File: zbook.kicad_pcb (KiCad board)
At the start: 4 copper layers, 77 x 89 mm, 170 parts, among them J1 USB_C_Receptacle_USB2.0_16P, J2 USB_C_Receptacle_USB2.0_16P, J3 Conn_01x05_Pin, J4 Conn_01x05_Pin, J5 Conn_02x04_Odd_Even, J6 Conn_02x15_Counter_Clockwise, J7 MSD-4-A, J8 DISPLAY CONN, Q1 T2N7002AK,LM, Q2 FDN327N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

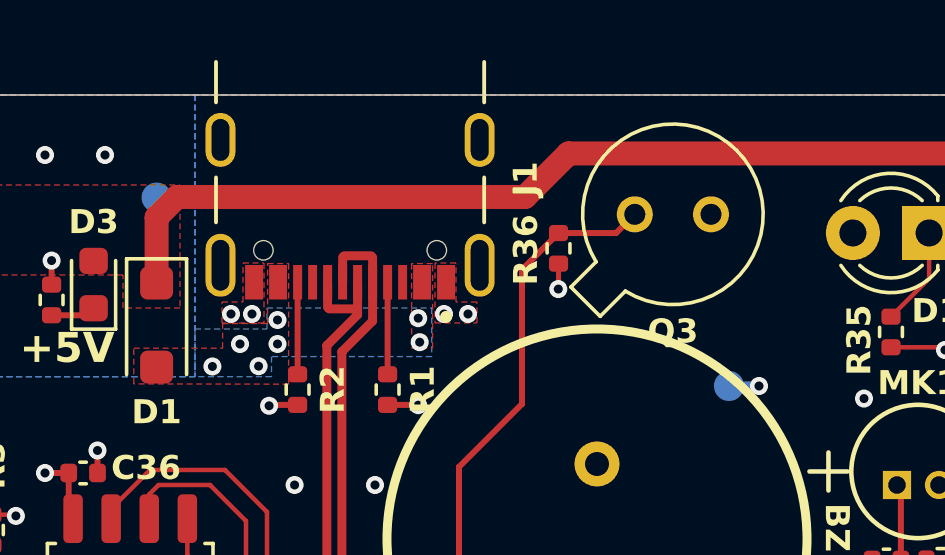
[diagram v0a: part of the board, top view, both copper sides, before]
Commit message: fix: changes phototransistor footprint
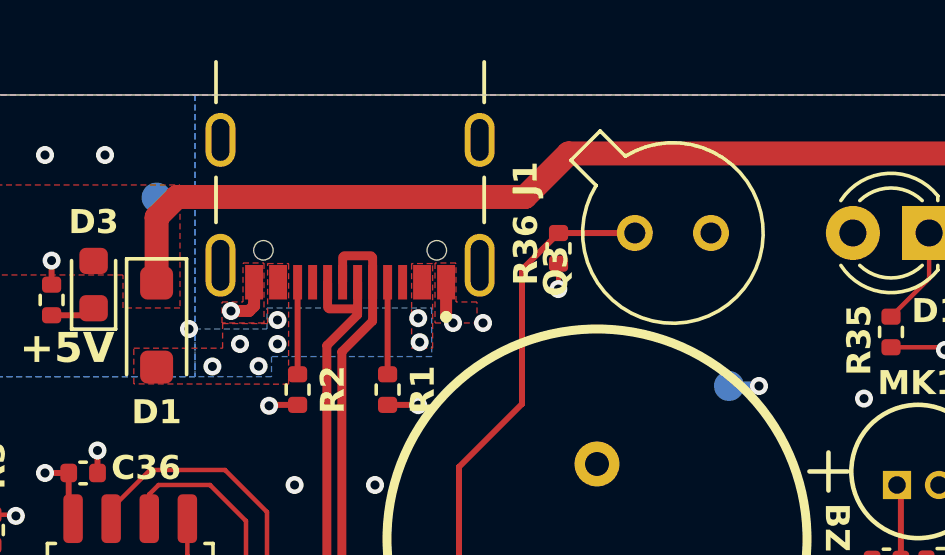
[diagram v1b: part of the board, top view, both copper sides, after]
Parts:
- moved Q3 1.41 mm to (155.9, 68.6), turned to -90 degrees
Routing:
- net GND: track 109.5 -> 112.6 mm
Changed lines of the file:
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@@
 	(footprint "peripherals1:TO-18-2"
 		(layer "F.Cu")
-		(at 154.66 67.978039)
+		(at 155.93 68.6 -90)
 		(descr "TO-18-2, generated with kicad-footprint-generator TO_SOT_THT_generate.py")
 		(tags "TO-18-2")
 		(property "Reference" "Q3"
-			(at 1.27 3.9 0)
+			(at 1.27 3.9 90)
 			(layer "F.SilkS")
 			(effects
@@
 		)
 		(property "Value" "Q_Photo_NPN"
-			(at 1.27 4.01 0)
+			(at 1.27 4.01 90)
 			(layer "F.Fab")
 			(effects
@@
 			)
 		)
-		(property "Datasheet" "https://www.digikey.com.br/pt/products/detail/tt-electronics-optek-technology/OP598A/498701?s=N4IgTCBcDaIPIAUCsBOAHAQRAXQL5A"
-			(at 0 0 0)
+		(property "Datasheet" "https://www.digikey.com.br/en/products/detail/tt-electronics-optek-technology/OP598A/498701?s=N4IgTCBcDaIPIAUCsBOAHAQRAXQL5A"
+			(at 0 0 90)
 			(layer "F.Fab")
 			(hide yes)
@@
 			)
 		)
-		(property "Description" "Phototransistor"
-			(at 0 0 0)
+		(property "Description" "NPN phototransistor, collector/emitter"
+			(at 0 0 90)
 			(layer "F.Fab")
 			(hide yes)
@@
 		)
 		(property "MPN" "OP598A"
-			(at 0 0 0)
+			(at 0 0 270)
 			(unlocked yes)
 			(layer "F.Fab")
@@
 		)
 		(property "Availability" ""
-			(at 0 0 0)
+			(at 0 0 270)
 			(unlocked yes)
 			(layer "F.Fab")
@@
 		)
 		(property "Check_prices" ""
-			(at 0 0 0)
+			(at 0 0 270)
 			(unlocked yes)
 			(layer "F.Fab")
@@
 		)
 		(property "Description_1" ""
-			(at 0 0 0)
+			(at 0 0 270)
 			(unlocked yes)
 			(layer "F.Fab")
@@
 		)
 		(property "MF" ""
-			(at 0 0 0)
+			(at 0 0 270)
 			(unlocked yes)
 			(layer "F.Fab")
@@
 		)
 		(property "Package" ""
-			(at 0 0 0)
+			(at 0 0 270)
 			(unlocked yes)
 			(layer "F.Fab")
@@
 		)
 		(property "Price" ""
-			(at 0 0 0)
+			(at 0 0 270)
 			(unlocked yes)
 			(layer "F.Fab")
@@
 		)
 		(property "SnapEDA_Link" ""
-			(at 0 0 0)
+			(at 0 0 270)
 			(unlocked yes)
 			(layer "F.Fab")
@@
 		(attr through_hole)
 		(fp_line
-			(start -2.130108 2.424301)
-			(end -1.154301 3.400108)
+			(start -2.424301 3.400108)
+			(end -1.583811 2.559618)
 			(stroke
 				(width 0.12)
@@
 		)
 		(fp_line
-			(start -1.289618 1.583811)
-			(end -2.130108 2.424301)
+			(start -3.400108 2.424301)
+			(end -2.424301 3.400108)
 			(stroke
 				(width 0.12)
@@
 		)
 		(fp_line
-			(start -1.154301 3.400108)
-			(end -0.313811 2.559618)
+			(start -2.559618 1.583811)
+			(end -3.400108 2.424301)
 			(stroke
 				(width 0.12)
@@
 		)
 		(fp_arc
-			(start -1.289618 1.583811)
-			(mid 3.398392 -2.128392)
-			(end -0.313811 2.559618)
+			(start -2.559618 1.583811)
+			(mid 2.128392 -2.128392)
+			(end -1.583811 2.559618)
 			(stroke
 				(width 0.12)
@@
 		)
 		(fp_line
-			(start -2.323922 2.420125)
-			(end -1.150125 3.593922)
+			(start -2.420125 3.593922)
+			(end -1.561775 2.735573)
 			(stroke
 				(width 0.05)
@@
 		)
 		(fp_line
-			(start -1.465573 1.561775)
-			(end -2.323922 2.420125)
+			(start -3.593922 2.420125)
+			(end -2.420125 3.593922)
 			(stroke
 				(width 0.05)
@@
 		)
 		(fp_line
-			(start -1.150125 3.593922)
-			(end -0.291775 2.735573)
+			(start -2.735573 1.561775)
+			(end -3.593922 2.420125)
 			(stroke
 				(width 0.05)
@@
 		)
 		(fp_arc
-			(start -1.465573 1.561775)
-			(mid 3.497386 -2.227386)
-			(end -0.291775 2.735573)
+			(start -2.735573 1.561775)
+			(mid 2.227386 -2.227386)
+			(end -1.561775 2.735573)
 			(stroke
 				(width 0.05)
@@
 		)
 		(fp_line
-			(start -1.976616 2.426372)
-			(end -1.156372 3.246616)
+			(start -2.426372 3.246616)
+			(end -1.599057 2.419301)
 			(stroke
 				(width 0.1)
@@
 		)
 		(fp_line
-			(start -1.156372 3.246616)
-			(end -0.329057 2.419301)
+			(start -3.246616 2.426372)
+			(end -2.426372 3.246616)
 			(stroke
 				(width 0.1)
@@
 		)
 		(fp_line
-			(start -1.149301 1.599057)
-			(end -1.976616 2.426372)
+			(start -2.419301 1.599057)
+			(end -3.246616 2.426372)
 			(stroke
 				(width 0.1)
@@
 		)
 		(fp_arc
-			(start -1.149301 1.599057)
-			(mid 3.32061 -2.05061)
-			(end -0.329057 2.419301)
+			(start -2.419301 1.599057)
+			(mid 2.05061 -2.05061)
+			(end -1.599057 2.419301)
 			(stroke
 				(width 0.1)
@@
 		)
 		(fp_circle
-			(center 1.27 0)
-			(end 3.67 0)
+			(center 0 0)
+			(end 2.4 0)
 			(stroke
 				(width 0.1)
@@
 		)
 		(fp_text user "${REFERENCE}"
-			(at 1.27 -4.01 0)
+			(at 1.27 -4.01 90)
 			(layer "F.Fab")
 			(effects
@@
 		)
 		(pad "1" thru_hole circle
-			(at 2.54 0)
+			(at 0 -1.27 270)
 			(size 1.2 1.2)
 			(drill 0.7)
@@
 			(pinfunction "C")
 			(pintype "passive")
-			(zone_connect 1)
 		)
 		(pad "2" thru_hole circle
-			(at 0 0)
+			(at 0 1.27 270)
 			(size 1.2 1.2)
 			(drill 0.7)
@@
 		)
 		(embedded_fonts no)
-		(model "${KICAD9_3DMODEL_DIR}/Package_TO_SOT_THT.3dshapes/TO-18-2.step"
+		(model "${KIPRJMOD}/Libraries/Peripherals1/OP598A.STEP"
 			(offset
-				(xyz 0 0 0)
+				(xyz 0 0 2)
 			)
 			(scale
@@
 			)
 			(rotate
-				(xyz 0 0 0)
+				(xyz -90 -0 -0)
 			)
 		)
@@
 	)
 	(segment
+		(start 148.37 71.37)
+		(end 148.6 71.6)
+		(width 0.4)
+		(layer "F.Cu")
+		(net 1)
+	)
+	(segment
+		(start 141.8 71.2)
+		(end 141.2 71.2)
+		(width 0.4)
+		(layer "F.Cu")
+		(net 1)
+	)
+	(segment
 		(start 144.785 106.055)
 		(end 144.74 106.01)
@@
 	)
 	(segment
+		(start 148.37 70.2425)
+		(end 148.37 71.37)
+		(width 0.4)
+		(layer "F.Cu")
+		(net 1)
+	)
+	(segment
 		(start 146.87 142.39)
 		(end 146.88 142.38)
@@
 	)
 	(segment
+		(start 141.97 70.2425)
+		(end 141.97 71.03)
+		(width 0.4)
+		(layer "F.Cu")
+		(net 1)
+	)
+	(segment
 		(start 137.28 101.05)
 		(end 136.55 101.05)
@@
 	)
 	(segment
+		(start 141.97 71.03)
+		(end 141.8 71.2)
+		(width 0.4)
+		(layer "F.Cu")
+		(net 1)
+	)
+	(segment
 		(start 128.950001 73.1)
 		(end 128.950001 74.430966)
@@
 	)
 	(via
-		(at 141.2 71.3)
+		(at 139.8 71.8)
 		(size 0.6)
 		(drill 0.3)
@@
 	)
 	(via
-		(at 141.9 71.3)
+		(at 141.2 71.2)
 		(size 0.6)
 		(drill 0.3)
@@
 	)
 	(via
-		(at 149.1 71.3)
+		(at 149.6 71.6)
 		(size 0.6)
 		(drill 0.3)
@@
 	)
 	(via
-		(at 148.3 71.3)
+		(at 148.6 71.6)
 		(size 0.6)
 		(drill 0.3)
@@
 	)
 	(segment
-		(start 152.118039 68.601961)
-		(end 154.036078 68.601961)
-		(width 0.2)
-		(layer "F.Cu")
-		(net 109)
-	)
-	(segment
 		(start 151.6 88.3)
 		(end 151.6 86.75)
@@
 	)
 	(segment
-		(start 154.036078 68.601961)
-		(end 154.66 67.978039)
+		(start 154.658039 68.601961)
+		(end 154.66 68.6)
+		(width 0.2)
+		(layer "F.Cu")
+		(net 109)
+	)
+	(segment
+		(start 152.118039 68.601961)
+		(end 154.658039 68.601961)
 		(width 0.2)
 		(layer "F.Cu")

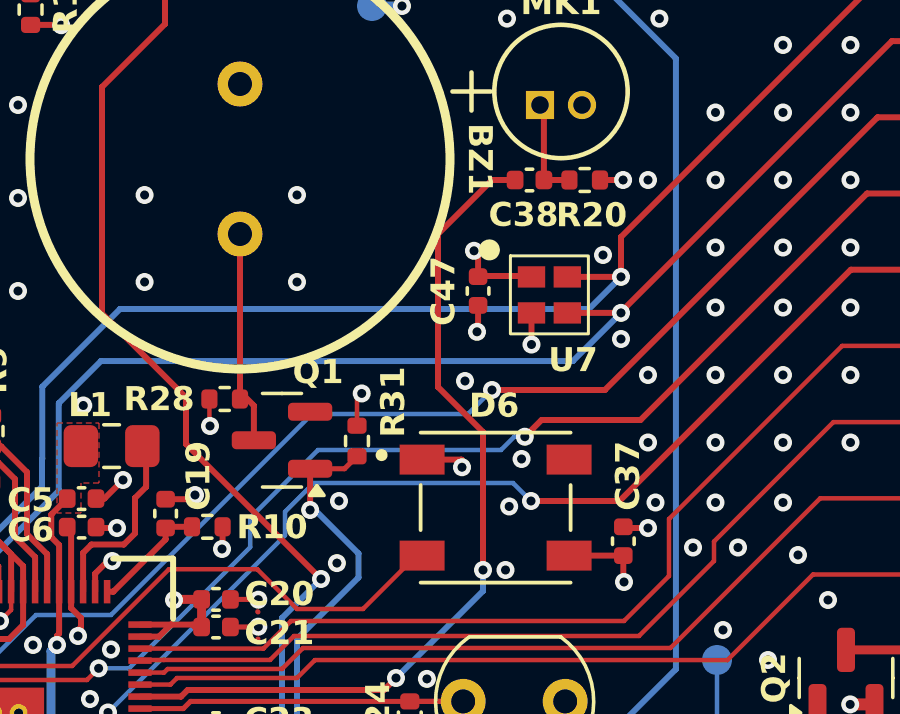
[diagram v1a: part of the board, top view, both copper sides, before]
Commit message: fix: fixes header table behind pcb
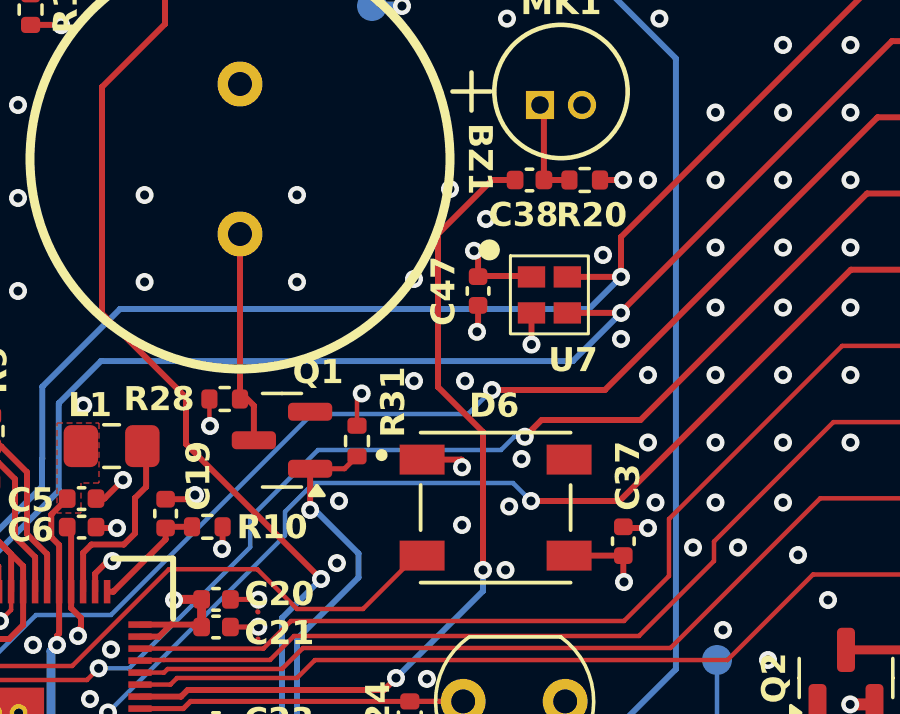
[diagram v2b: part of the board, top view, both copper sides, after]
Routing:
- net GND: vias 414 -> 419
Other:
- board text added: "Front Header View"
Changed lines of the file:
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@@
 		)
 	)
+	(gr_text "Front Header View"
+		(at 176.2 100.8 0)
+		(layer "B.SilkS")
+		(effects
+			(font
+				(size 1 1)
+				(thickness 0.2)
+				(bold yes)
+			)
+			(justify left bottom mirror)
+		)
+	)
 	(gr_text "ZBook Project\nGerber Files:\n- Comments Layer: zbook-User_Comments.gbr\n- PCB Edge Cut Layer: zbook-Edge_Cuts.gbr\n- Front Copper Layer: zbook-F_Cu.gbr\n- Front Solder Mask Layer: zbook-F_Mask.gbr\n- Front Solder Paste Layer: zbook-F_Paste.gbr\n- Front Silkscreen Layer: zbook-F_Silkscreen.gbr\n- Inner 1 Layer: zbook-In1_Cu.gbr\n- Inner 2 Layer: zbook-In2_Cu.gbr\n- Bottom Copper Layer: zbook-B_Cu.gbr\n- Bottom Solder Mask Layer: zbook-B_Mask.gbr\n- Bottom Solder Paste Layer: zbook-B_Paste.gbr\n- Bottom Silkscreen Layer: zbook-B_Silkscreen.gbr"
 		(at 191.8 86.5 0)
@@
 			)
 		)
-		(column_widths 7.325 13.2)
-		(row_heights 1.9 1.8 1.9 1.8 1.9 2 1.9 1.6 1.9 1.8 1.9 2 1.9 2)
+		(column_widths 7.2 13.2)
+		(row_heights 1.65 1.8 1.8 1.8 1.8 1.8 1.8 1.8 1.8 1.8 1.8 1.8 1.8 1.8 1.8)
 		(cells
 			(table_cell "+3V3"
-				(start 155.3375 100.85)
-				(end 162.6625 102.75)
+				(start 155.4 101.175)
+				(end 162.6 102.825)
 				(margins 1.0025 1.0025 1.0025 1.0025)
 				(span 1 1)
@@
 			)
 			(table_cell "+VBUS"
-				(start 162.6625 100.85)
-				(end 175.8625 102.75)
+				(start 162.6 101.175)
+				(end 175.8 102.825)
 				(margins 1.0025 1.0025 1.0025 1.0025)
 				(span 1 1)
@@
 			)
 			(table_cell "GND"
-				(start 155.3375 102.75)
-				(end 162.6625 104.55)
+				(start 155.4 102.825)
+				(end 162.6 104.625)
 				(margins 1.0025 1.0025 1.0025 1.0025)
 				(span 1 1)
@@
 				)
 			)
-			(table_cell "I2C SCL"
-				(start 162.6625 102.75)
-				(end 175.8625 104.55)
+			(table_cell "I2C_SCL"
+				(start 162.6 102.825)
+				(end 175.8 104.625)
 				(margins 1.0025 1.0025 1.0025 1.0025)
 				(span 1 1)
@@
 			)
 			(table_cell "GND"
-				(start 155.3375 104.55)
-				(end 162.6625 106.45)
+				(start 155.4 104.625)
+				(end 162.6 106.425)
+				(margins 1.0025 1.0025 1.0025 1.0025)
+				(span 1 1)
+				(layer "B.SilkS")
+				(effects
+					(font
+						(size 1 1)
+						(thickness 0.2)
+					)
+					(justify left mirror)
+				)
+			)
+			(table_cell "I2C_SDA"
+				(start 162.6 104.625)
+				(end 175.8 106.425)
+				(margins 1.0025 1.0025 1.0025 1.0025)
+				(span 1 1)
+				(layer "B.SilkS")
+				(effects
+					(font
+						(size 1 1)
+						(thickness 0.2)
+					)
+					(justify left mirror)
+				)
+			)
+			(table_cell "GND"
+				(start 155.4 106.425)
+				(end 162.6 108.225)
 				(margins 1.0025 1.0025 1.0025 1.0025)
 				(span 1 1)
@@
 			)
 			(table_cell "GPIO08"
-				(start 162.6625 104.55)
-				(end 175.8625 106.45)
+				(start 162.6 106.425)
+				(end 175.8 108.225)
 				(margins 1.0025 1.0025 1.0025 1.0025)
 				(span 1 1)
@@
 			)
 			(table_cell "GND"
-				(start 155.3375 106.45)
-				(end 162.6625 108.25)
+				(start 155.4 108.225)
+				(end 162.6 110.025)
 				(margins 1.0025 1.0025 1.0025 1.0025)
 				(span 1 1)
@@
 			)
 			(table_cell "GPIO07"
-				(start 162.6625 106.45)
-				(end 175.8625 108.25)
+				(start 162.6 108.225)
+				(end 175.8 110.025)
 				(margins 1.0025 1.0025 1.0025 1.0025)
 				(span 1 1)
@@
 			)
 			(table_cell "GND"
-				(start 155.3375 108.25)
-				(end 162.6625 110.15)
+				(start 155.4 110.025)
+				(end 162.6 111.825)
 				(margins 1.0025 1.0025 1.0025 1.0025)
 				(span 1 1)
@@
 			)
 			(table_cell "GPIO43 (ADC)"
-				(start 162.6625 108.25)
-				(end 175.8625 110.15)
+				(start 162.6 110.025)
+				(end 175.8 111.825)
 				(margins 1.0025 1.0025 1.0025 1.0025)
 				(span 1 1)
@@
 			)
 			(table_cell "GND"
-				(start 155.3375 110.15)
-				(end 162.6625 112.15)
+				(start 155.4 111.825)
+				(end 162.6 113.625)
 				(margins 1.0025 1.0025 1.0025 1.0025)
 				(span 1 1)
@@
 			)
 			(table_cell "GPIO47 (ADC)"
-				(start 162.6625 110.15)
-				(end 175.8625 112.15)
+				(start 162.6 111.825)
+				(end 175.8 113.625)
 				(margins 1.0025 1.0025 1.0025 1.0025)
 				(span 1 1)
@@
 			)
 			(table_cell "GND"
-				(start 155.3375 112.15)
-				(end 162.6625 114.05)
+				(start 155.4 113.625)
+				(end 162.6 115.425)
 				(margins 1.0025 1.0025 1.0025 1.0025)
 				(span 1 1)
@@
 			)
 			(table_cell "GPIO46 (ADC)"
-				(start 162.6625 112.15)
-				(end 175.8625 114.05)
+				(start 162.6 113.625)
+				(end 175.8 115.425)
 				(margins 1.0025 1.0025 1.0025 1.0025)
 				(span 1 1)
@@
 			)
 			(table_cell "GND"
-				(start 155.3375 114.05)
-				(end 162.6625 115.65)
+				(start 155.4 115.425)
+				(end 162.6 117.225)
 				(margins 1.0025 1.0025 1.0025 1.0025)
 				(span 1 1)
@@
 			)
 			(table_cell "GPIO45 (ADC)"
-				(start 162.6625 114.05)
-				(end 175.8625 115.65)
+				(start 162.6 115.425)
+				(end 175.8 117.225)
 				(margins 1.0025 1.0025 1.0025 1.0025)
 				(span 1 1)
@@
 			)
 			(table_cell "GND"
-				(start 155.3375 115.65)
-				(end 162.6625 117.55)
+				(start 155.4 117.225)
+				(end 162.6 119.025)
 				(margins 1.0025 1.0025 1.0025 1.0025)
 				(span 1 1)
@@
 			)
 			(table_cell "GPIO44 (ADC)"
-				(start 162.6625 115.65)
-				(end 175.8625 117.55)
+				(start 162.6 117.225)
+				(end 175.8 119.025)
 				(margins 1.0025 1.0025 1.0025 1.0025)
 				(span 1 1)
@@
 			)
 			(table_cell "GND"
-				(start 155.3375 117.55)
-				(end 162.6625 119.35)
+				(start 155.4 119.025)
+				(end 162.6 120.825)
 				(margins 1.0025 1.0025 1.0025 1.0025)
 				(span 1 1)
@@
 				)
 			)
-			(table_cell "MOSFET DRAIN"
-				(start 162.6625 117.55)
-				(end 175.8625 119.35)
+			(table_cell "MOSFET_DRAIN"
+				(start 162.6 119.025)
+				(end 175.8 120.825)
 				(margins 1.0025 1.0025 1.0025 1.0025)
 				(span 1 1)
@@
 			)
 			(table_cell "GND"
-				(start 155.3375 119.35)
-				(end 162.6625 121.25)
+				(start 155.4 120.825)
+				(end 162.6 122.625)
 				(margins 1.0025 1.0025 1.0025 1.0025)
 				(span 1 1)
@@
 				)
 			)
-			(table_cell "SPI MISO"
-				(start 162.6625 119.35)
-				(end 175.8625 121.25)
+			(table_cell "SPI_MISO"
+				(start 162.6 120.825)
+				(end 175.8 122.625)
 				(margins 1.0025 1.0025 1.0025 1.0025)
 				(span 1 1)
@@
 			)
 			(table_cell "GPIO27"
-				(start 155.3375 121.25)
-				(end 162.6625 123.25)
+				(start 155.4 122.625)
+				(end 162.6 124.425)
 				(margins 1.0025 1.0025 1.0025 1.0025)
 				(span 1 1)
@@
 			)
 			(table_cell "GPIO26"
-				(start 162.6625 121.25)
-				(end 175.8625 123.25)
+				(start 162.6 122.625)
+				(end 175.8 124.425)
 				(margins 1.0025 1.0025 1.0025 1.0025)
 				(span 1 1)
@@
 			)
 			(table_cell "GND"
-				(start 155.3375 123.25)
-				(end 162.6625 125.15)
+				(start 155.4 124.425)
+				(end 162.6 126.225)
 				(margins 1.0025 1.0025 1.0025 1.0025)
 				(span 1 1)
@@
 				)
 			)
-			(table_cell "SPI SCLK"
-				(start 162.6625 123.25)
-				(end 175.8625 125.15)
+			(table_cell "SPI_SCLK"
+				(start 162.6 124.425)
+				(end 175.8 126.225)
 				(margins 1.0025 1.0025 1.0025 1.0025)
 				(span 1 1)
@@
 			)
 			(table_cell "GND"
-				(start 155.3375 125.15)
-				(end 162.6625 127.15)
+				(start 155.4 126.225)
+				(end 162.6 128.025)
 				(margins 1.0025 1.0025 1.0025 1.0025)
 				(span 1 1)
@@
 				)
 			)
-			(table_cell "SPI MOSI"
-				(start 162.6625 125.15)
-				(end 175.8625 127.15)
+			(table_cell "SPI_MOSI"
+				(start 162.6 126.225)
+				(end 175.8 128.025)
 				(margins 1.0025 1.0025 1.0025 1.0025)
 				(span 1 1)
@@
 	)
 	(via
+		(at 160.4 79.8)
+		(size 0.6)
+		(drill 0.3)
+		(layers "F.Cu" "B.Cu")
+		(free yes)
+		(net 1)
+	)
+	(via
 		(at 132.9 90.3)
 		(size 0.6)
@@
 	)
 	(via
+		(at 160.8 91)
+		(size 0.6)
+		(drill 0.3)
+		(layers "F.Cu" "B.Cu")
+		(free yes)
+		(net 1)
+	)
+	(via
 		(at 161.3 136.4)
 		(size 0.6)
@@
 	)
 	(via
+		(at 159.2 82.8)
+		(size 0.6)
+		(drill 0.3)
+		(layers "F.Cu" "B.Cu")
+		(free yes)
+		(net 1)
+	)
+	(via
 		(at 137.2 117.1)
 		(size 0.6)
@@
 	)
 	(via
+		(at 159.2 86.2)
+		(size 0.6)
+		(drill 0.3)
+		(layers "F.Cu" "B.Cu")
+		(free yes)
+		(net 1)
+	)
+	(via
 		(at 163 129.92)
 		(size 0.6)
@@
 		(size 0.6)
 		(drill 0.3)
+		(layers "F.Cu" "B.Cu")
+		(free yes)
+		(net 1)
+	)
+	(via
+		(at 161.6 80.8)
+		(size 0.6)
+		(drill 0.3)

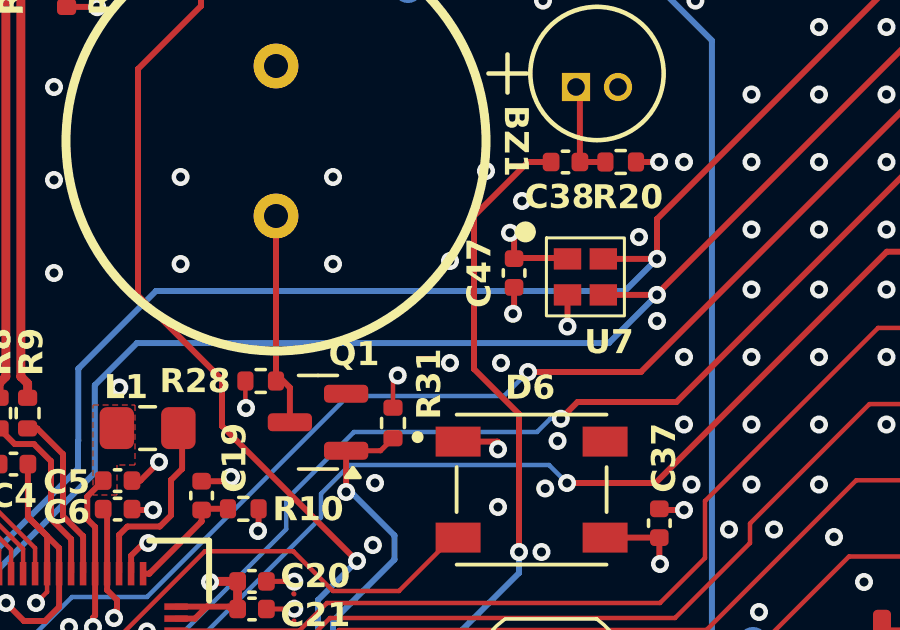
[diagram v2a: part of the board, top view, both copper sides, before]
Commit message: refac: adds one more via for shielding an analog trace
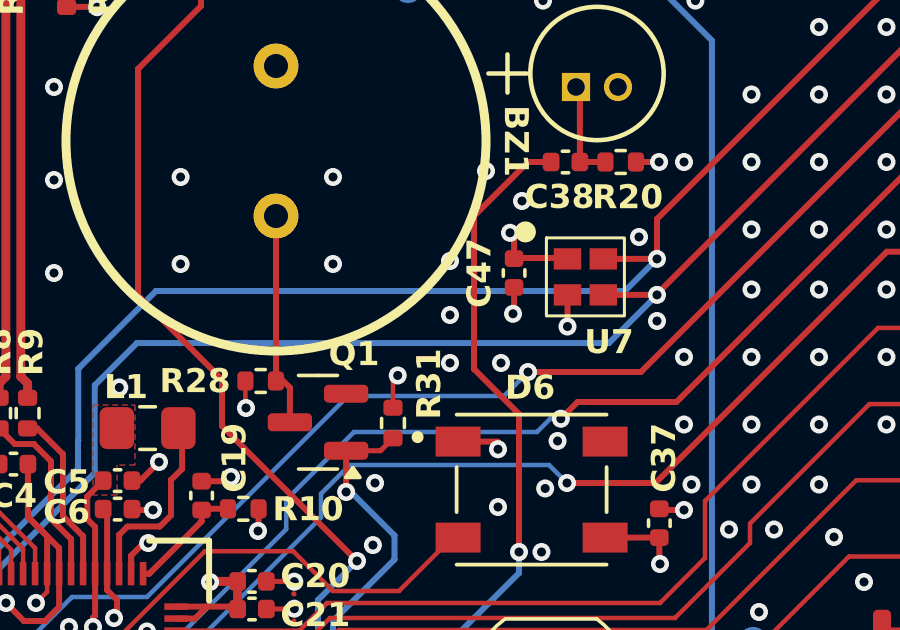
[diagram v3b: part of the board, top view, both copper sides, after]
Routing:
- net GND: vias 419 -> 420
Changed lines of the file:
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@@
+	)
+	(via
+		(at 159.2 84.6)
+		(size 0.6)
+		(drill 0.3)
+		(layers "F.Cu" "B.Cu")
+		(free yes)
+		(net 1)
 	)
 	(via
